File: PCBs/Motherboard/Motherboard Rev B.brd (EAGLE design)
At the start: 95.9 x 90.2 mm, 64 parts, among them J1 MOLEX_504050-0591, J2 MOLEX_504050-0491, Q1 16M, Q2 32.768k, U1 Value, X1 2514-5

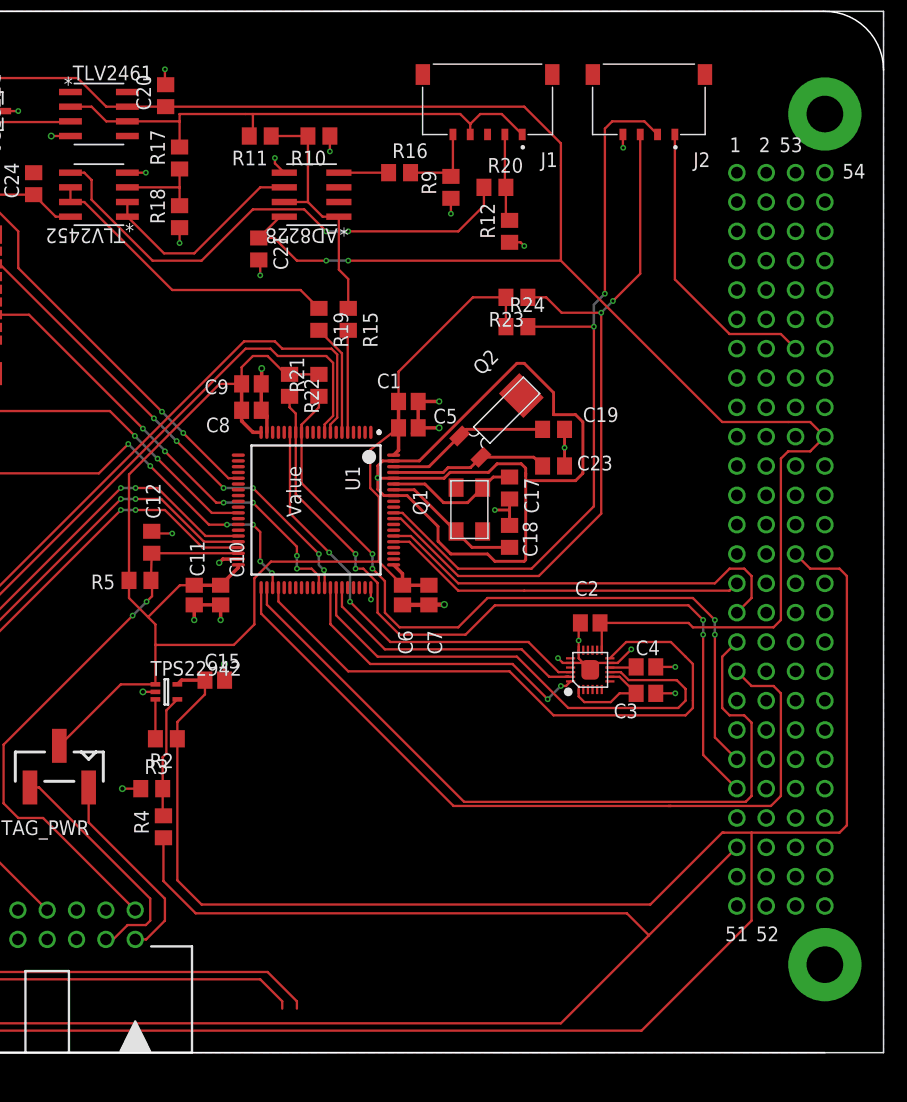
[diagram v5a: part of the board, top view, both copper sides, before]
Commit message: Add external 5V charging jack
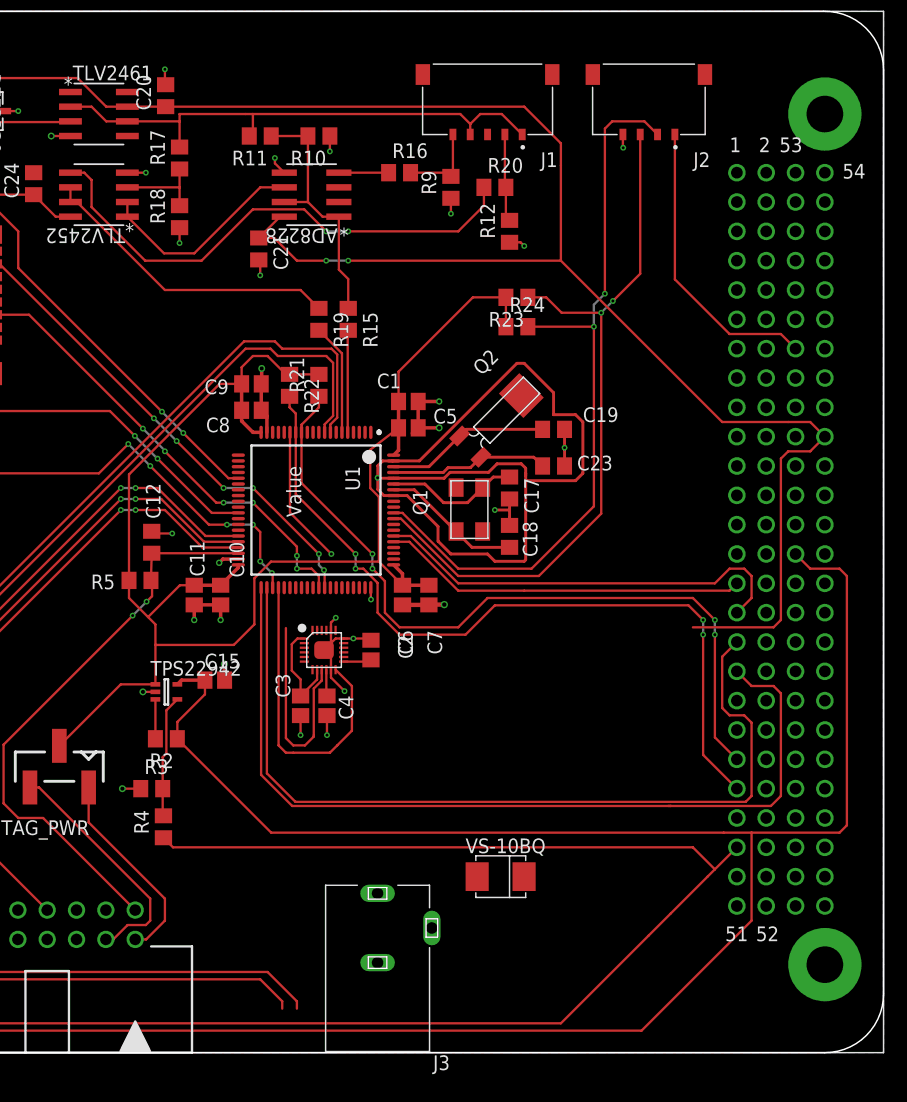
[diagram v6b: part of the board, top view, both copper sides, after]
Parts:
- added J3: PJ-102A, PJ-102A:CUI_PJ-102A
- added VS-10BQ: 10BQ015HM3, Vishay 10BQ015HM3:SMB
- moved C3 29.9 mm to (45.4, 30.0), turned to 270 degrees
- moved C4 27.8 mm to (47.7, 30.0), turned to 270 degrees
- moved U$2 23.1 mm to (47.4, 34.9), turned to 0 degrees
- moved C2 19.1 mm to (51.5, 34.9), turned to 90 degrees
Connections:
- new net 5V_CHG: U$1.32, VS-10BQ.C
- new net N$14: J3.1, VS-10BQ.A
- net GND: now also J3.2, J3.3
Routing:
- net MOSI_IMU: track 27.3 -> 0.00 mm, vias 2 -> 0
- net INT_IMU: track 53.8 -> 26.9 mm
- net CS_IMU: track 38.4 -> 12.0 mm, vias 2 -> 1
- net MISO_IMU: track 44.4 -> 18.6 mm
- net CLK_IMU: track 24.2 -> 0.20 mm
- net 3V3: track 248.0 -> 235.6 mm
- net PINAVL1_TX: track 66.4 -> 74.9 mm
- net SW10: track 191.8 -> 183.6 mm
- net PINAVL1_RX: track 68.2 -> 76.4 mm
- net LI_OA_RESET: track 168.1 -> 169.2 mm
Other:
- outline, holes or cut-outs redrawn

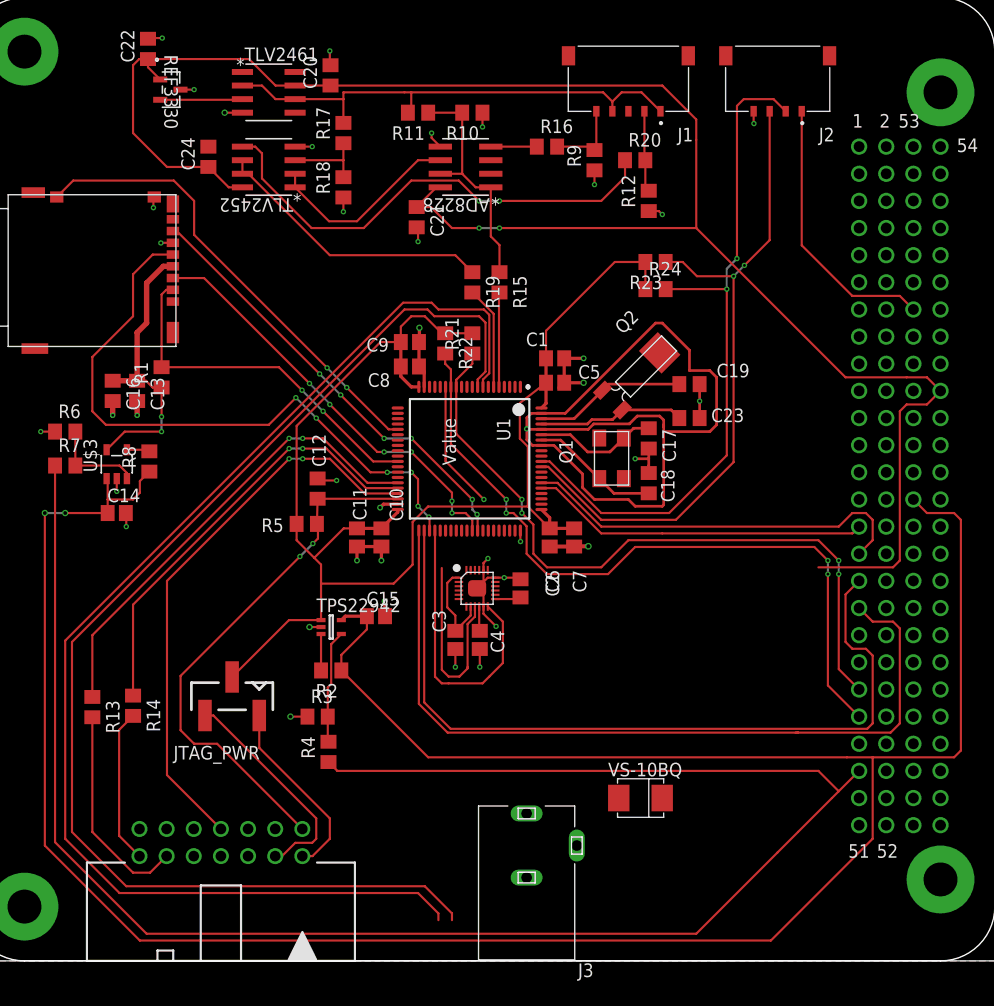
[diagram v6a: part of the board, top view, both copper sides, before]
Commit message: Swap JTAG UART and piNAV comm channels
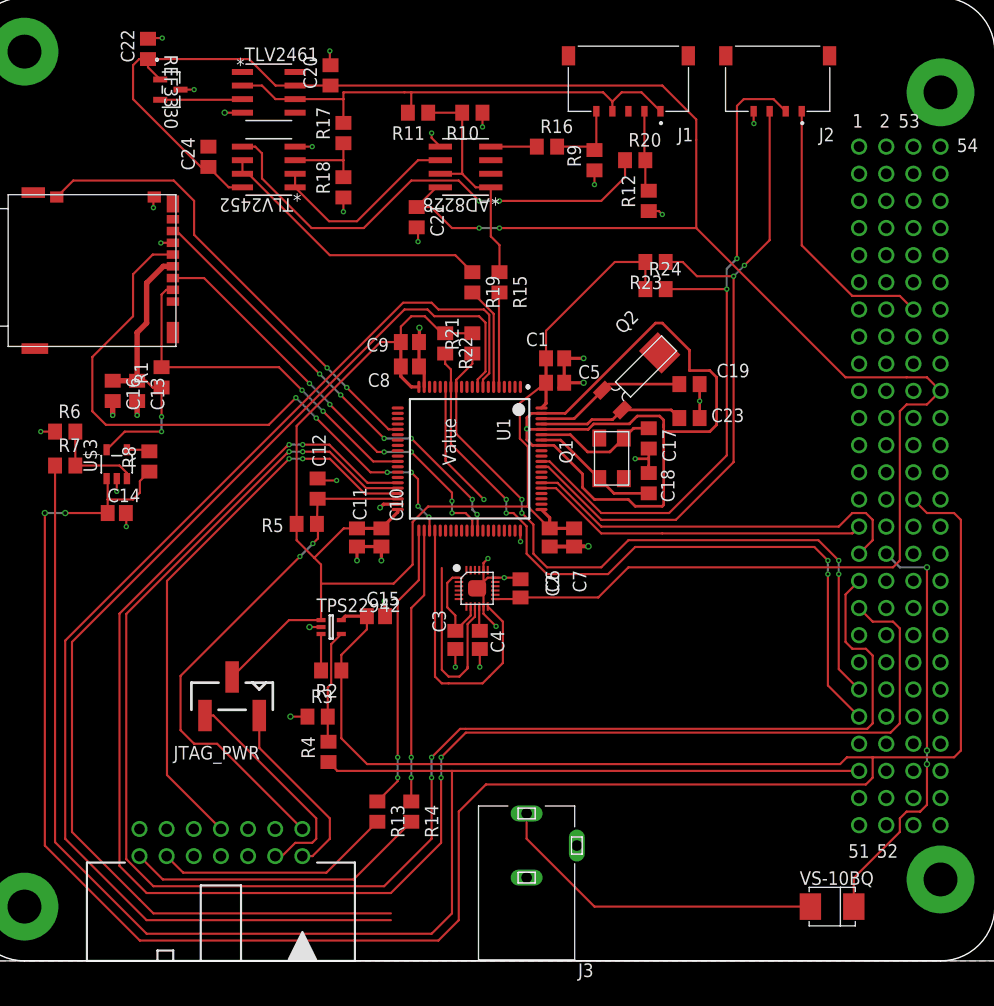
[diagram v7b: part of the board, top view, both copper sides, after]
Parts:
- moved R13 28.4 mm to (38.1, 14.0)
- moved R14 27.9 mm to (41.3, 14.0)
- moved VS-10BQ 23.3 mm to (80.6, 5.08)
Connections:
- net JTAG_RXD: now also U1.41; no longer U1.35
- net JTAG_TXD: now also U1.42; no longer U1.36
- net PINAVL1_RX: now also U1.35; no longer U1.41
- net PINAVL1_TX: now also U1.36; no longer U1.42
- net SCL_ANT: no longer U$1.39
- net SDA_ANT: no longer U$1.37
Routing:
- net PINAVL1_RX: track 76.4 -> 156.5 mm, vias 0 -> 4
- net PINAVL1_TX: track 74.9 -> 153.4 mm, vias 0 -> 4
- net 5V_CHG: track 0.00 -> 39.7 mm, vias 0 -> 3
- net N$14: track 0.00 -> 31.6 mm
- net LI_OA_RESET: track 169.2 -> 140.1 mm
- net SW10: track 183.6 -> 210.8 mm
- net JTAG_RXD: track 43.7 -> 27.0 mm
- net JTAG_TXD: track 40.9 -> 25.8 mm
- net N$8: track 14.4 -> 28.6 mm
- net 3V3: track 235.6 -> 242.5 mm
- net EXT_TXD: track 115.5 -> 109.2 mm
- net EXT_RXD: track 117.2 -> 112.4 mm
- net N$11: track 19.9 -> 22.3 mm
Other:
- board text added: "Route these around SD"

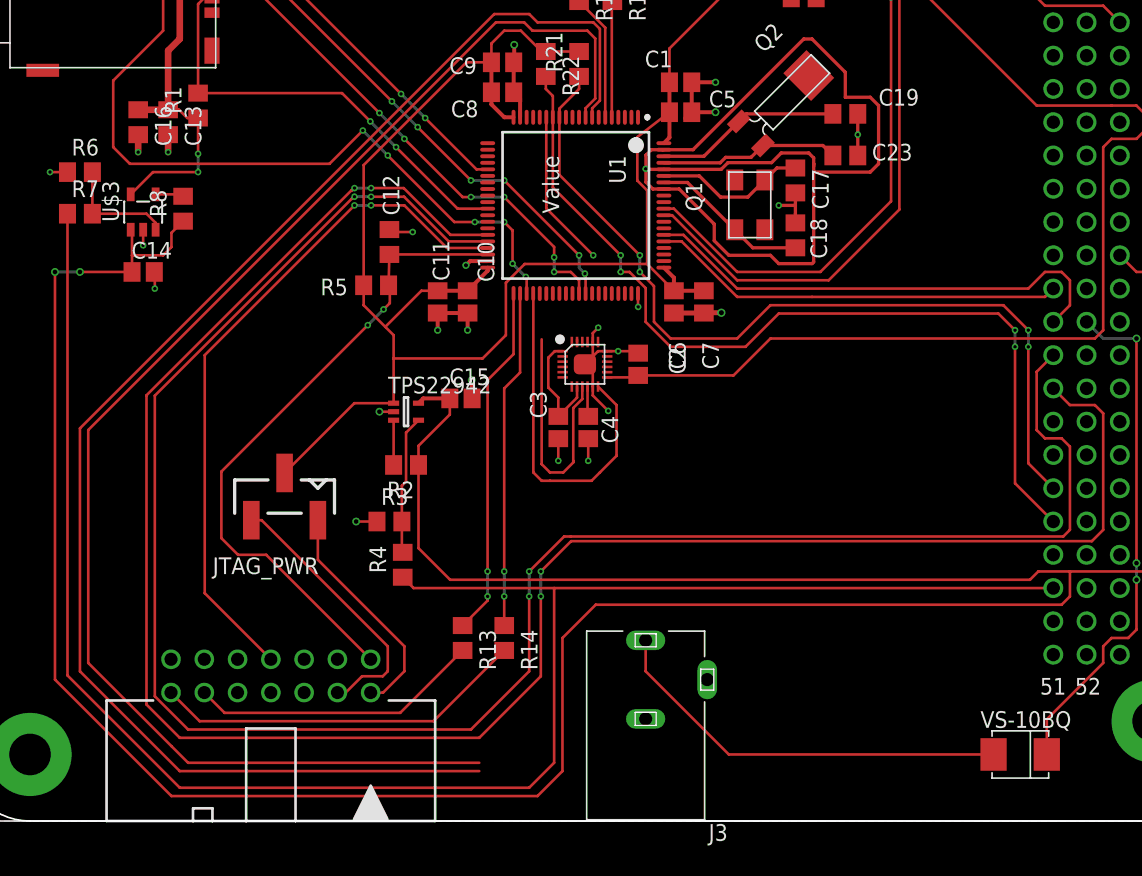
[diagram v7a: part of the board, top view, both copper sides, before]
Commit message: Add external UART connector
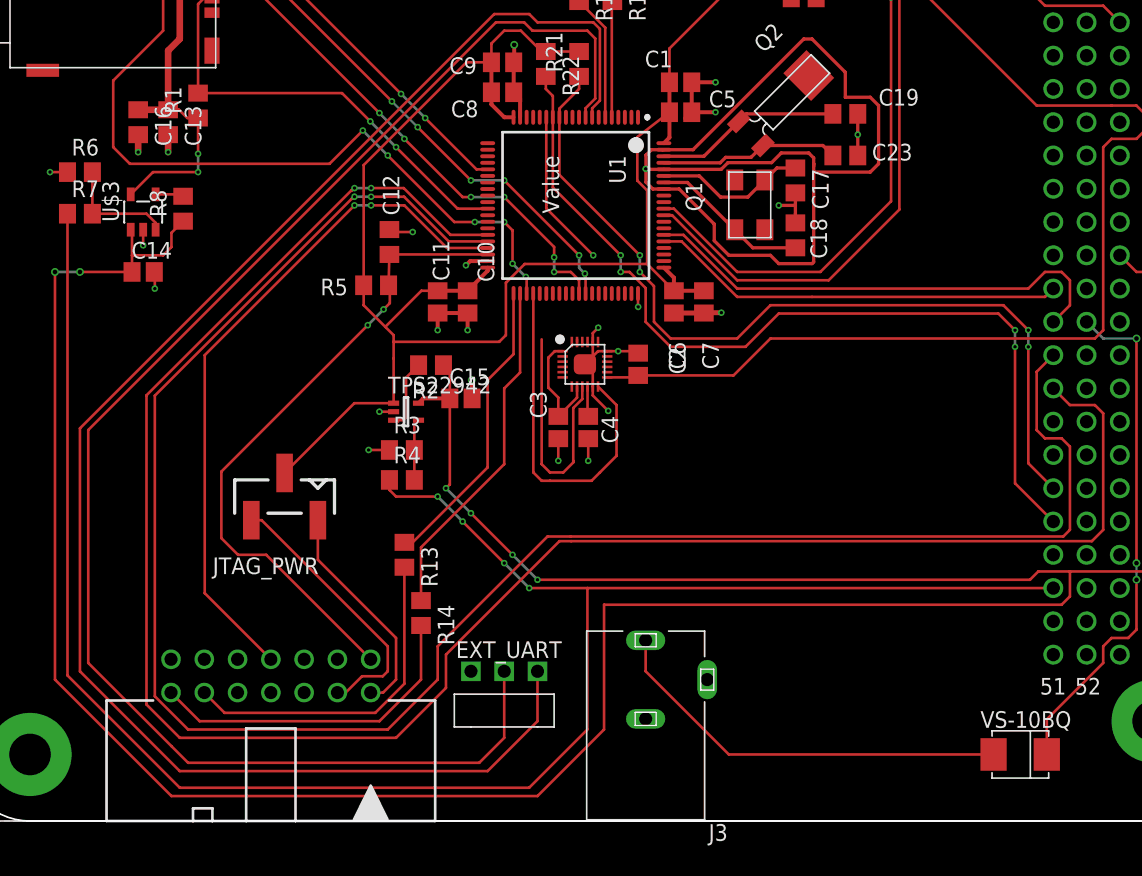
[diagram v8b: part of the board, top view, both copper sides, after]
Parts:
- added EXT_UART: 90121-0763, Molex 90121-0763:90121-0763
- moved R2 7.85 mm to (35.7, 34.8)
- moved R13 7.75 mm to (33.7, 20.3)
- moved R14 6.63 mm to (34.9, 15.9)
- moved R4 6.48 mm to (33.5, 26.0), turned to 0 degrees
- moved R3 5.54 mm to (33.5, 28.3)
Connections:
- net EXT_RXD: now also EXT_UART.3
- net EXT_TXD: now also EXT_UART.2
- net GND: now also EXT_UART.1
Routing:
- net EXT_RXD: track 112.4 -> 122.3 mm
- net EXT_TXD: track 109.2 -> 117.0 mm
- net N$5: track 10.6 -> 4.69 mm
- net LI_OA_RESET: track 140.1 -> 145.7 mm, vias 0 -> 4
- net JTAG_RXD: track 27.0 -> 22.8 mm, vias 2 -> 0
- net N$11: track 22.3 -> 25.7 mm
- net 3V3: track 242.5 -> 239.2 mm, vias 2 -> 6
- net PINAVL1_RX: track 156.5 -> 153.3 mm, vias 4 -> 2
- net N$8: track 28.6 -> 25.4 mm
- net PINAVL1_TX: track 153.4 -> 150.4 mm, vias 4 -> 2
- net N$1: track 3.41 -> 5.43 mm
- net JTAG_TXD: track 25.8 -> 26.6 mm, vias 2 -> 0
- net 3V3_UC: track 134.3 -> 133.8 mm
- net VCC_TOOL: track 17.5 -> 17.0 mm
